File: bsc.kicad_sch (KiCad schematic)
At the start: 74 parts, among them J1 Conn_JTAG_ESP, J2 Prog, J3 Conn_Extension, J4 Boot, J6 JP_U3TX_EN, Q1 BC857BS, Q12 IRLML2244, Q13 BC857BS, Q14 IRLML2244, U1 LMO78_03-0.5, U13 ADuM1201AR, U19 LMO78_05-0.5, U2 ESP32WROOM32E16, U7 SN65HVD234, X1 Conn_S2, X4 Conn_SV

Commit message: Ref 2.4
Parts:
- removed JP28: 12V_5V, Jumper:SolderJumper-2_P1.3mm_Open_RoundedPad1.0x1.5mm, symbol Jumper:SolderJumper_2_Open
- removed JP30: JP_EXT_5V, Jumper:SolderJumper-2_P1.3mm_Open_RoundedPad1.0x1.5mm, symbol Jumper:SolderJumper_2_Open
- removed JP31: JP_EXT_3V3, Jumper:SolderJumper-2_P1.3mm_Open_RoundedPad1.0x1.5mm, symbol Jumper:SolderJumper_2_Open
- removed PS1: 1S4E_0503S1U, custom_th:Converter_DCDC_GAPTEC_1S4E_S1U, symbol Converter_DCDC:MEE1S0303SC
- removed X1: Conn_S2, Connector_Phoenix_MC:PhoenixContact_MCV_1,5_9-G-3.81_1x09_P3.81mm_Vertical, symbol Connector:Conn_01x09_Male
- added JP28: 12V_5V, Jumper:SolderJumper-2_P1.3mm_Bridged_RoundedPad1.0x1.5mm, symbol Jumper:SolderJumper_2_Bridged
- added JP30: JP_EXT_5V, Jumper:SolderJumper-2_P1.3mm_Bridged_RoundedPad1.0x1.5mm, symbol Jumper:SolderJumper_2_Bridged
- added JP31: JP_EXT_3V3, Jumper:SolderJumper-2_P1.3mm_Bridged_RoundedPad1.0x1.5mm, symbol Jumper:SolderJumper_2_Bridged
- added PS1: (no value), symbol lcsc:B0503S-1WR2_C5127059
- added X1: Conn_S2, Connector_Phoenix_MC:PhoenixContact_MCV_1,5_6-G-3.81_1x06_P3.81mm_Vertical, symbol Connector:Conn_01x06_Male
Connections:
- net +3V3: now also JP31.1 (A), X1.2 (Pin_2)
- net +5V: now also JP28.1 (A), JP30.1 (A), PS1.2 (VIN)
- net CAN_GND: now also PS1.3 (0V), X1.6 (Pin_6)
- net CAN_H: now also X1.4 (Pin_4)
- net CAN_L: now also X1.5 (Pin_5)
- net CAN_VCC: now also PS1.4 (+VO)
- net GND: now also PS1.1 (GND), X1.1 (Pin_1)
- net V_IN: now also JP28.2 (B)
- net onewire: now also X1.3 (Pin_3)
- net at J3.8 (Pin_8): now also JP30.2 (B)
- net at J3.7 (Pin_7): now also JP31.2 (B)
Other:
- sheet serial ports: added none; removed U1RX_O, U1TX_O, U1_GND, U1_VCC_e
- note added: "Alternativbestückung 5V/12V - Wenn 12V intern benötigt werden U19 bestücken und JP28 auftrennen. - Werden keine 12V benötigt U19 NICHT bestücken."
- note removed: "Alternativbestückung 5V/12V - Wenn 12V intern benötigt werden U19 bestücken. - Werden keine 12V benötigt U19 NICHT bestücken und mit JP28 überbrücken."
- moved on the sheet: C10, C11, C12, R19

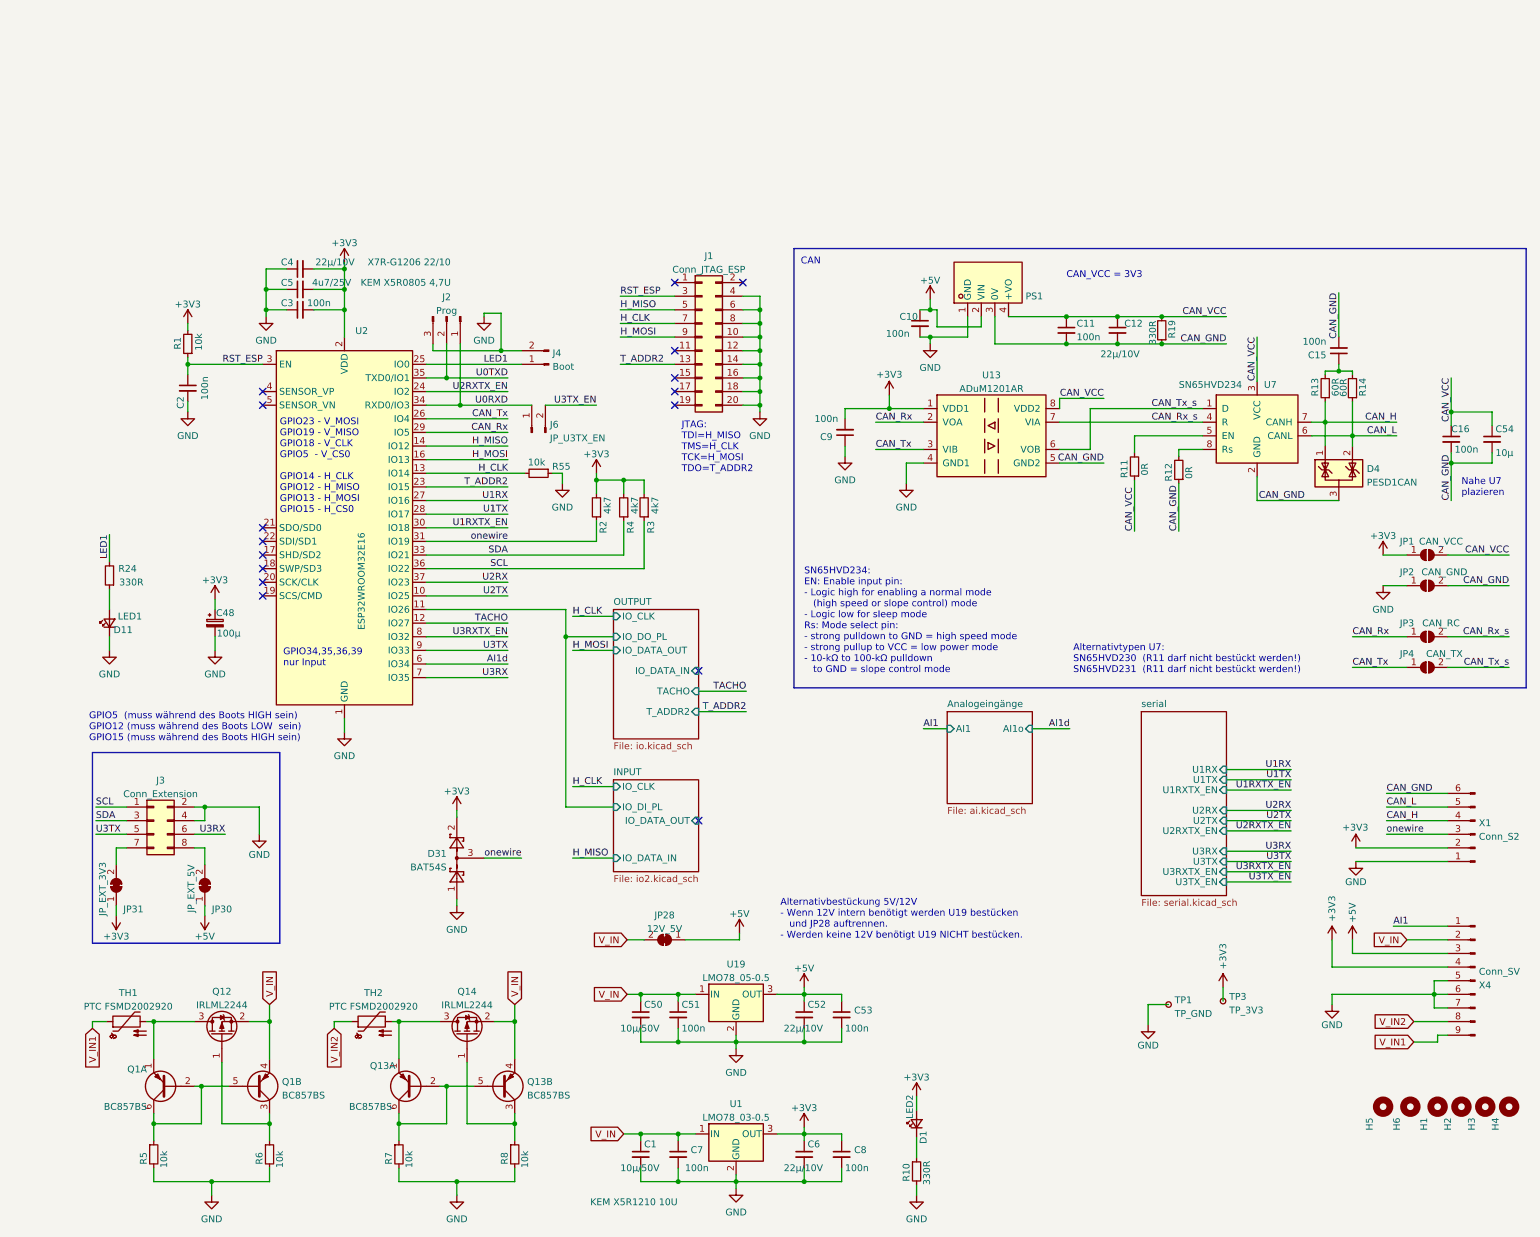
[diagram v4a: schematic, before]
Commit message: Improvements added (Ref 2.4.1)
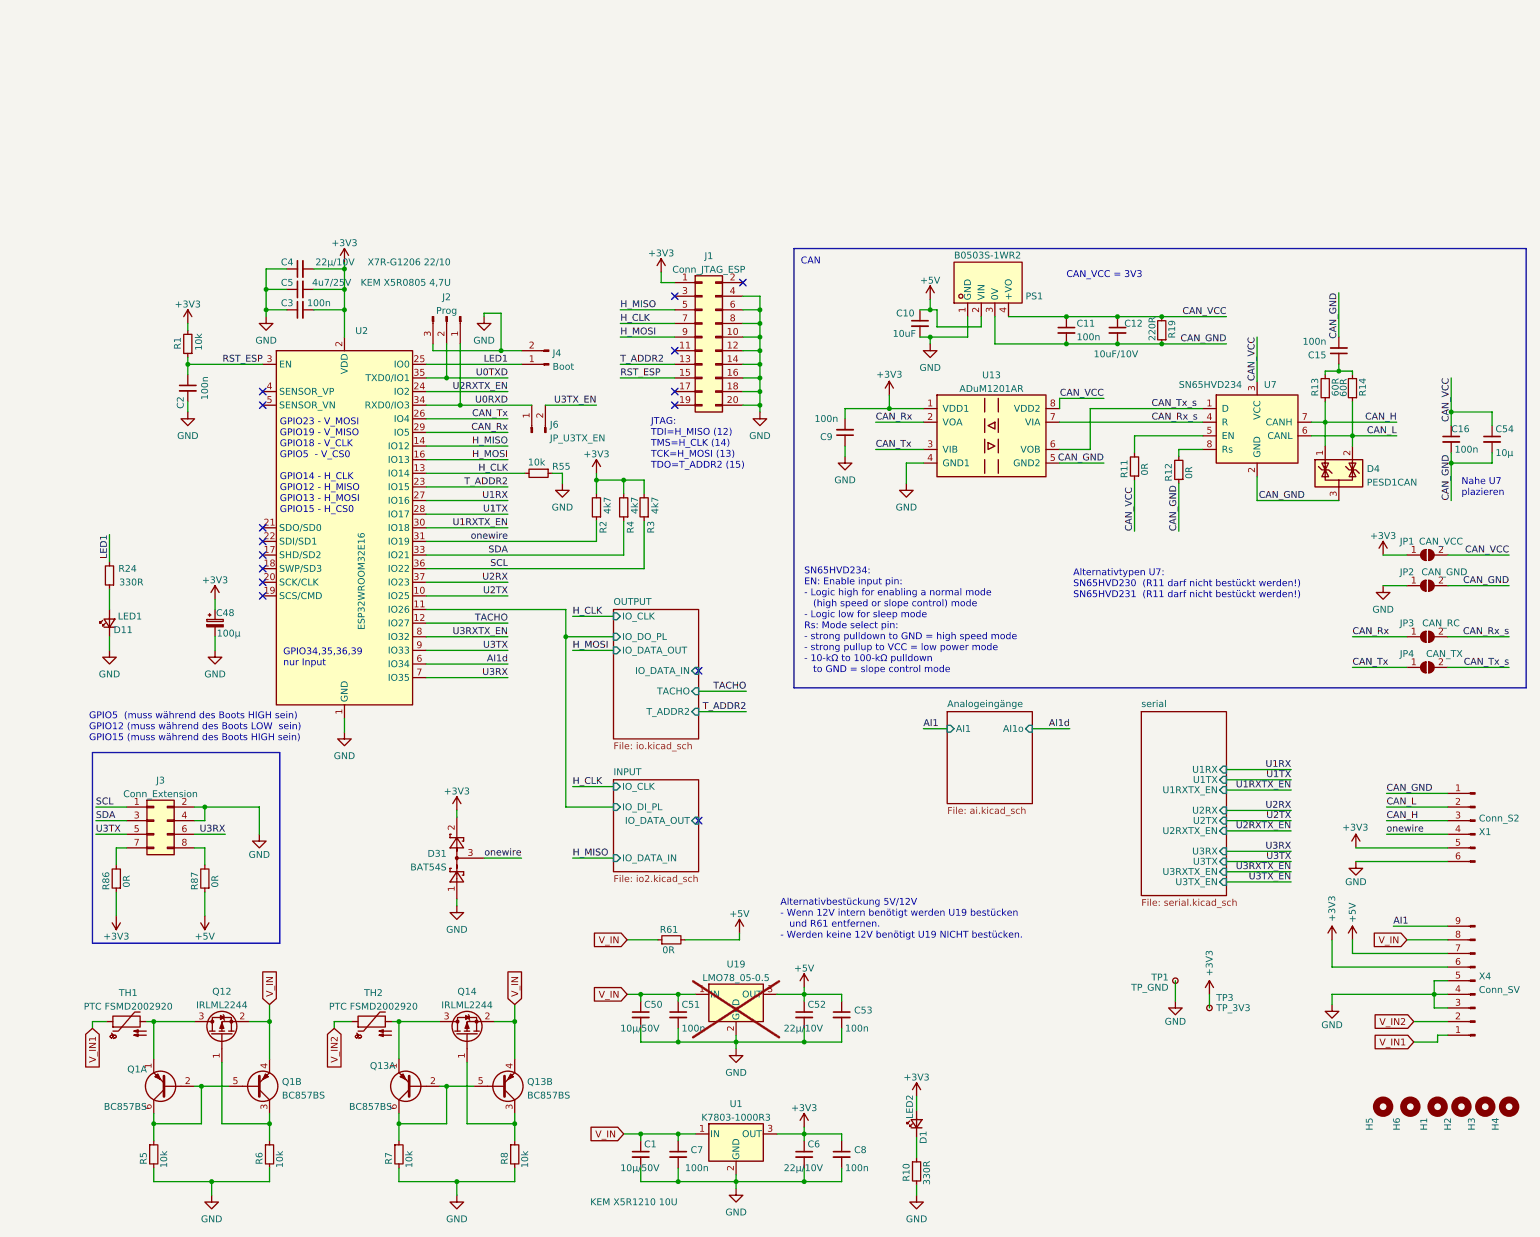
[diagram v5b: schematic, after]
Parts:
- removed JP28: 12V_5V, Jumper:SolderJumper-2_P1.3mm_Bridged_RoundedPad1.0x1.5mm, symbol Jumper:SolderJumper_2_Bridged
- removed JP30: JP_EXT_5V, Jumper:SolderJumper-2_P1.3mm_Bridged_RoundedPad1.0x1.5mm, symbol Jumper:SolderJumper_2_Bridged
- removed JP31: JP_EXT_3V3, Jumper:SolderJumper-2_P1.3mm_Bridged_RoundedPad1.0x1.5mm, symbol Jumper:SolderJumper_2_Bridged
- added R61, R86, R87: 0R, Resistor_SMD:R_0603_1608Metric, symbol Device:R_Small
- C10: value 100n -> 10uF
- C12: value 22µ/10V -> 10uF/10V
- PS1: value (none) -> B0503S-1WR2; footprint (none) -> lcsc:PWRM-TH_DEXU_BXXXXS-1WR2
- R19: value 330R -> 220R; footprint Resistor_SMD:R_0603_1608Metric -> Resistor_SMD:R_0805_2012Metric
- U1: value LMO78_03-0.5 -> K7803-1000R3; LCSC Part (none) -> C111278
- U19: now not fitted
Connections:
- net +3V3: now also J1.1 (Pin_1), X1.5 (Pin_5), X4.6 (Pin_6), R86.1; no longer X1.2 (Pin_2), X4.4 (Pin_4)
- net +5V: now also X4.7 (Pin_7), R61.2, R87.1; no longer X4.3 (Pin_3)
- net AI1: now also X4.9 (Pin_9); no longer X4.1 (Pin_1)
- net CAN_GND: now also X1.1 (Pin_1); no longer X1.6 (Pin_6)
- net CAN_H: now also X1.3 (Pin_3); no longer X1.4 (Pin_4)
- net CAN_L: now also X1.2 (Pin_2); no longer X1.5 (Pin_5)
- net GND: now also X1.6 (Pin_6), X4.3 (Pin_3), X4.4 (Pin_4); no longer X1.1 (Pin_1), X4.6 (Pin_6), X4.7 (Pin_7)
- net RST_ESP: now also J1.15 (Pin_15); no longer J1.3 (Pin_3)
- net V_IN: now also X4.8 (Pin_8), R61.1; no longer X4.2 (Pin_2)
- net V_IN1: now also X4.1 (Pin_1); no longer X4.9 (Pin_9)
- net V_IN2: now also X4.2 (Pin_2); no longer X4.8 (Pin_8)
- net onewire: now also X1.4 (Pin_4); no longer X1.3 (Pin_3)
- net at J3.8 (Pin_8): now also R87.2
- net at J3.7 (Pin_7): now also R86.2
- no-connect marks 16 -> 15
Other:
- note added: "Alternativbestückung 5V/12V - Wenn 12V intern benötigt werden U19 bestücken und R61 entfernen. - Werden keine 12V benötigt U19 NICHT bestücken."
- note added: "JTAG: TDI=H_MISO (12) TMS=H_CLK (14) TCK=H_MOSI (13) TDO=T_ADDR2 (15)"
- note removed: "Alternativbestückung 5V/12V - Wenn 12V intern benötigt werden U19 bestücken und JP28 auftrennen. - Werden keine 12V benötigt U19 NICHT bestücken."
- note removed: "JTAG: TDI=H_MISO TMS=H_CLK TCK=H_MOSI TDO=T_ADDR2"
- moved on the sheet: TP1, TP3, X1, X4

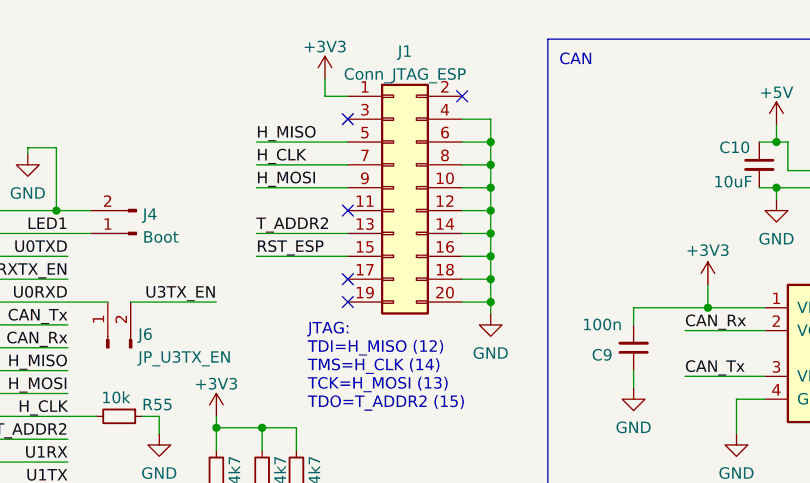
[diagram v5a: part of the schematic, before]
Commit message: Fix pullup
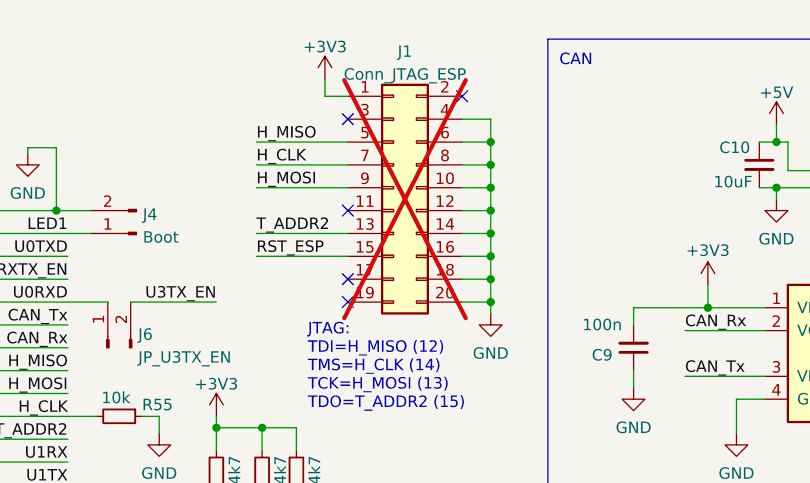
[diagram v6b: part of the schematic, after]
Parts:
- J1: now not fitted
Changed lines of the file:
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@@
   )
   (symbol (lib_id "Connector_Generic:Conn_02x10_Odd_Even") (at 128.905 31.75 0) (unit 1)
-    (in_bom yes) (on_board yes) (dnp no) (fields_autoplaced)
+    (in_bom yes) (on_board yes) (dnp yes) (fields_autoplaced)
     (property "Reference" "J1" (at 130.175 16.6202 0)
       (effects (font (size 1.27 1.27)))
@@
       (effects (font (size 1.27 1.27)) hide)
     )
+    (property "LCSC Part" "" (at 128.905 31.75 0)
+      (effects (font (size 1.27 1.27)) hide)
+    )
